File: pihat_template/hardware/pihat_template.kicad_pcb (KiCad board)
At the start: 2 copper layers, 65 x 56.5 mm, 37 parts, among them P1 CONN_01X02, P2 CONN_01X02, P3 Raspberry_Pi_+_Conn, Q1 BSS138, U1 LM3489, U2 CAT24C32HU4I-GT3, U3 FDC5614P, U4 LM1117IMPX-ADJ, U5 DMMT5401

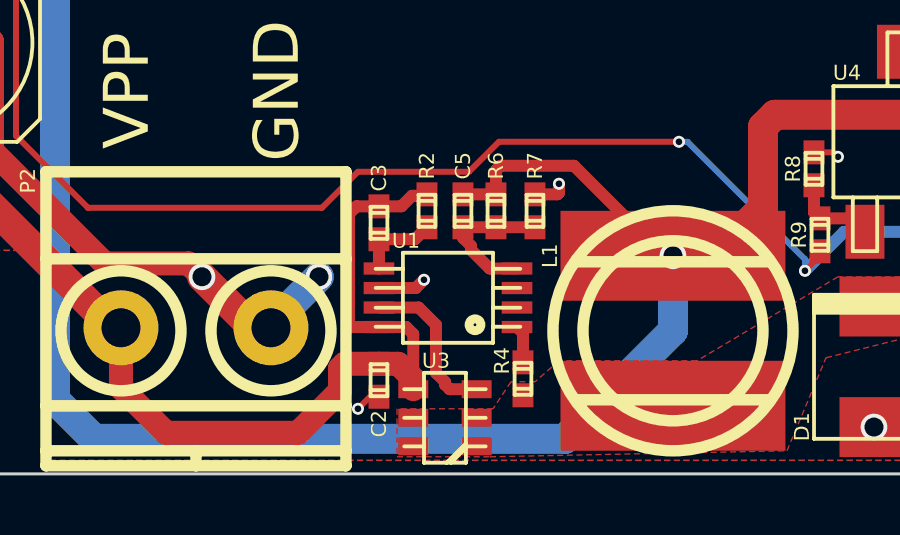
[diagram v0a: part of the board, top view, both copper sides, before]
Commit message: changed LM3489 footprint
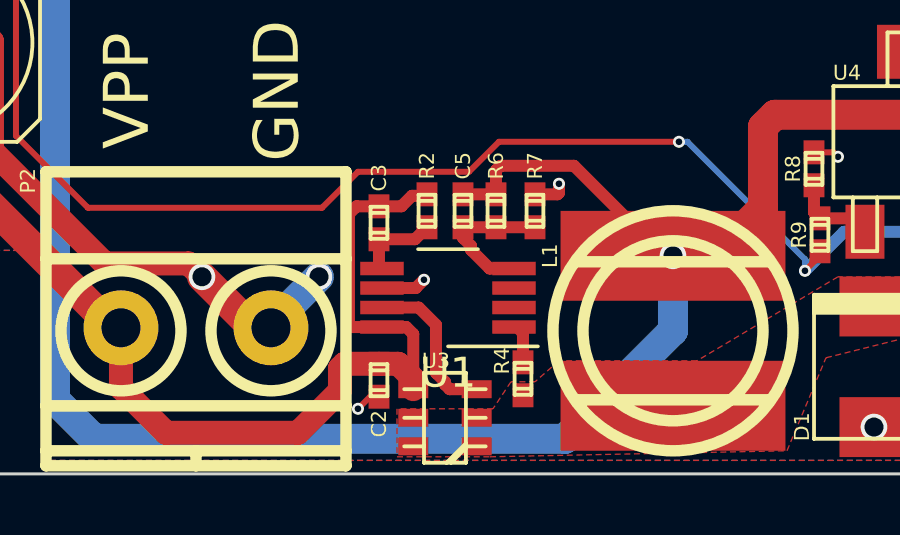
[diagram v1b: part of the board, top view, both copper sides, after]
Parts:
- U1: footprint w_smd_dil:msoic-8 -> kicad-gfa:VSSOP-8_3.0x3.0mm_Pitch0.65mm
- turned U1 to 180 degrees

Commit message: add VSSOP as a project footprint
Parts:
- U1: footprint kicad-gfa:VSSOP-8_3.0x3.0mm_Pitch0.65mm -> project:VSSOP-8_3.0x3.0mm_Pitch0.65mm
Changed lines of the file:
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@@
     )
   )
-  (module kicad-gfa:VSSOP-8_3.0x3.0mm_Pitch0.65mm (layer F.Cu)
+  (module project:VSSOP-8_3.0x3.0mm_Pitch0.65mm (layer F.Cu)
     (at 125.5 121.7 180)
     (descr "VSSOP-8 3.0 x 3.0, http://www.ti.com/lit/ds/symlink/lm75b.pdf")

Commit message: added silk UMONS-GFA + name
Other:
- board text added: "Julien M. - modified by UMONS-GFA"
- board text added: "pihat-template - 11/2017"
- board text removed: "Julien M."
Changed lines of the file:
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@@
     (area 104.1025 69.0525 177.679167 136.400001)
     (thickness 1.6)
-    (drawings 28)
+    (drawings 29)
     (tracks 280)
     (zones 0)
@@
     )
   )
+  (gr_text "pihat-template - 11/2017" (at 155.601 126.719) (layer F.SilkS)
+    (effects (font (size 0.75 0.75) (thickness 0.1875)))
+  )
   (gr_text "CERN OHL V1.2" (at 169.1 116 270) (layer B.SilkS)
     (effects (font (size 0.7 0.7) (thickness 0.175)) (justify mirror))
   )
-  (gr_text "Julien M." (at 169 116.6 90) (layer F.SilkS)
+  (gr_text "Julien M. - modified by UMONS-GFA" (at 168.8725 105.8275 90) (layer F.SilkS)
     (effects (font (size 1 1) (thickness 0.25)))
   )

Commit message: updated vias for EuroCircuits standards
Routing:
- net GND: track 44.4 -> 46.7 mm
- net Net-(JP1-Pad1): track 10.0 -> 11.5 mm
- net +3V3: track 176.1 -> 176.7 mm
- net Net-(P3-Pad28): track 32.4 -> 32.9 mm
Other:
- rule via_min_drill: 0.16 -> 0.3
- rule via_min_size: 0.26 -> 0.7

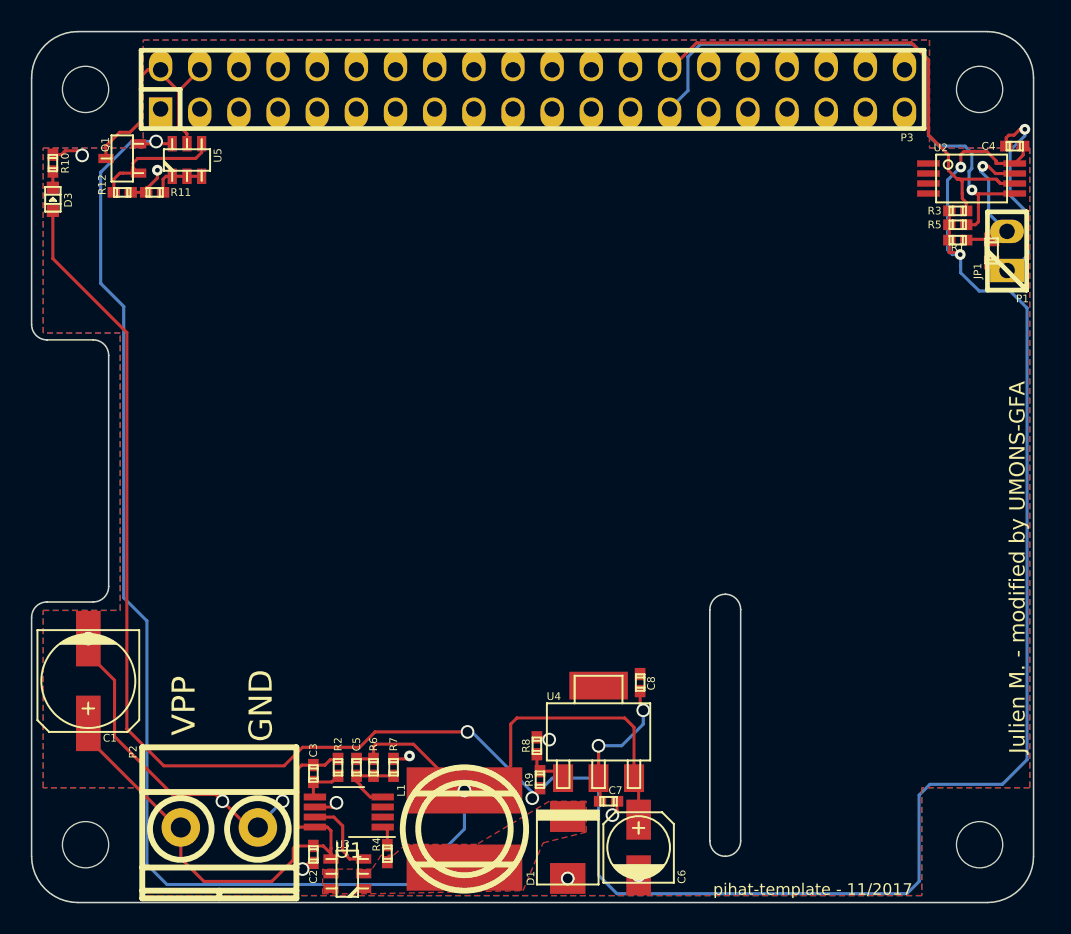
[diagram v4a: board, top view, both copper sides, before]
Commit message: added  and links to 3D models for modules in project lib
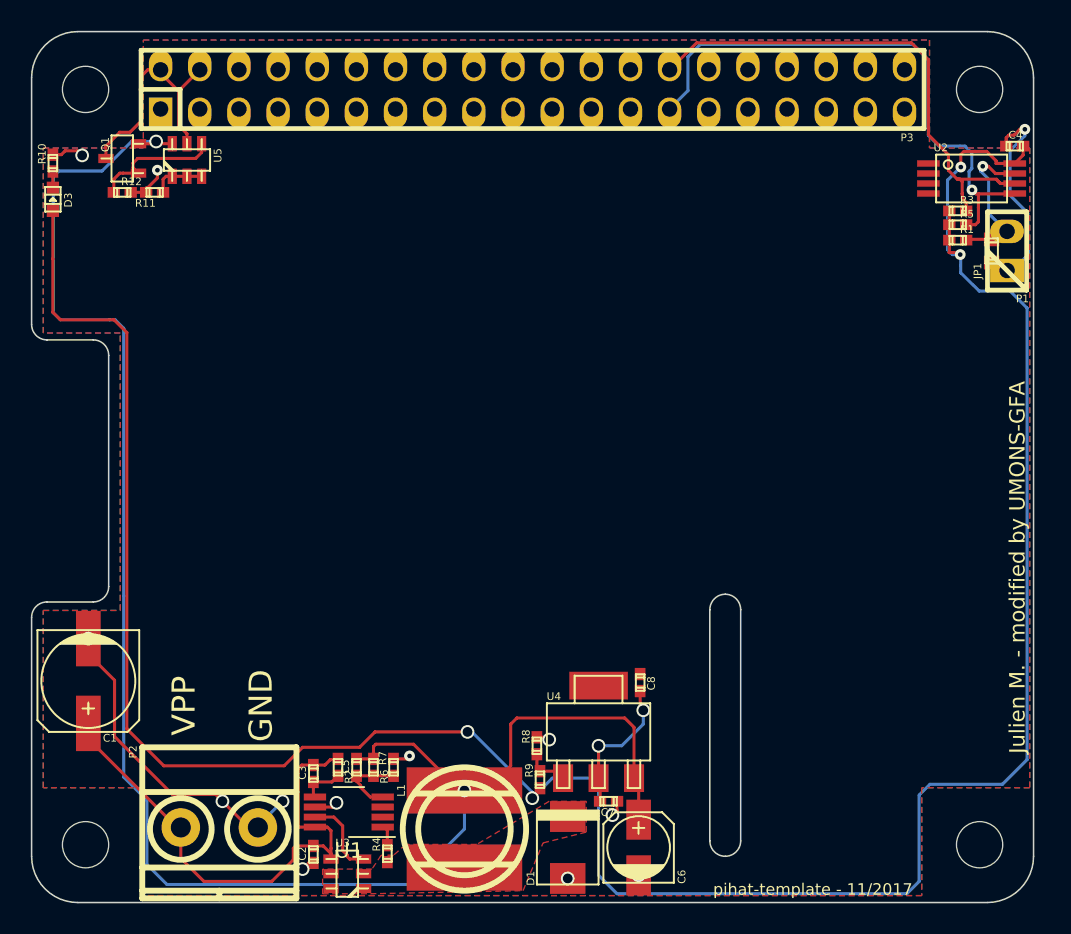
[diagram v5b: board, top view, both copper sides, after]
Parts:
- C1: footprint w_smd_cap:c_elec_6.3x7.7 -> project:c_elec_6.3x7.7
- C2, C3, C4, C5, C7, C8: footprint w_smd_cap:c_0402 -> project:c_0402
- C6: footprint w_smd_cap:c_elec_4x5.3 -> project:c_elec_4x5.3
- D1: footprint w_smd_diode:do214aa -> project:do214aa
- D3: footprint w_smd_leds:Led_0603 -> project:Led_0603
- L1: footprint w_smd_inductors:inductor_smd_8x5mm -> project:inductor_smd_8x5mm
- P1: footprint w_pin_strip:pin_strip_2 -> project:pin_strip_2
- P2: footprint w_conn_mkds:mkds_1,5-2 -> project:mkds_1,5-2
- P3: footprint w_pin_strip:pin_socket_20x2 -> project:pin_socket_20x2
- Q1: footprint w_smd_trans:sot23 -> project:sot23
- R1, R10, R11, R12, R2, R3, R4, R5, R6, R7, R8, R9: footprint w_smd_resistors:r_0402 -> project:r_0402
- U2: footprint w_smd_dil:tssop-8 -> project:tssop-8
- U3, U5: footprint w_smd_trans:sot23-6 -> project:sot23-6
- U4: footprint w_smd_trans:sot223 -> project:sot223
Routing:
- net +5V: track 108.0 -> 114.3 mm
- net +3V3: track 176.7 -> 178.7 mm

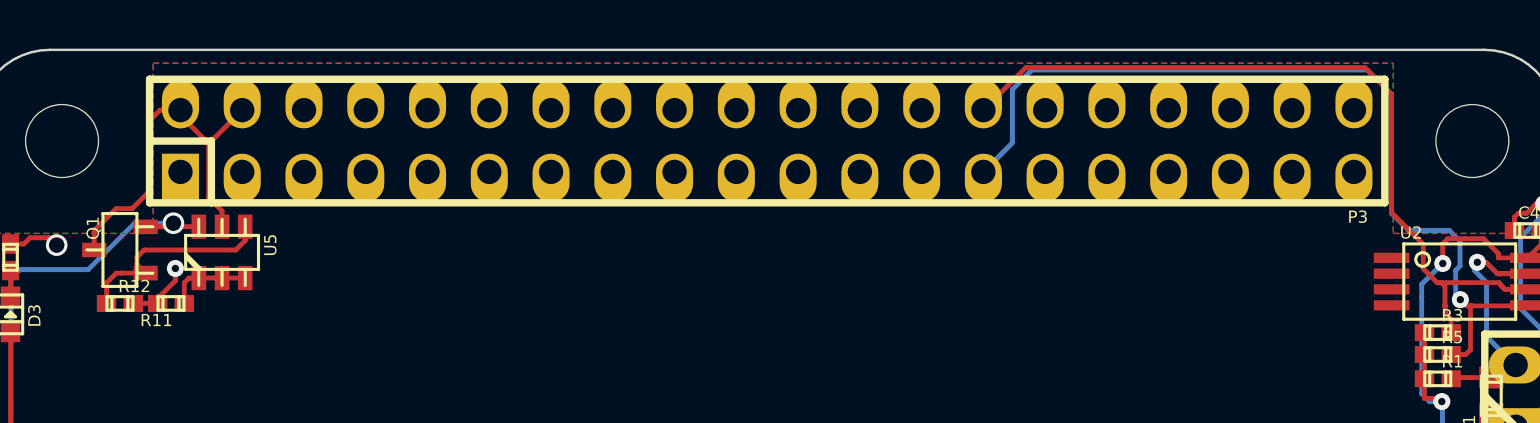
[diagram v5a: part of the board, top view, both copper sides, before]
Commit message: raspberry pi connector moved to back side of board
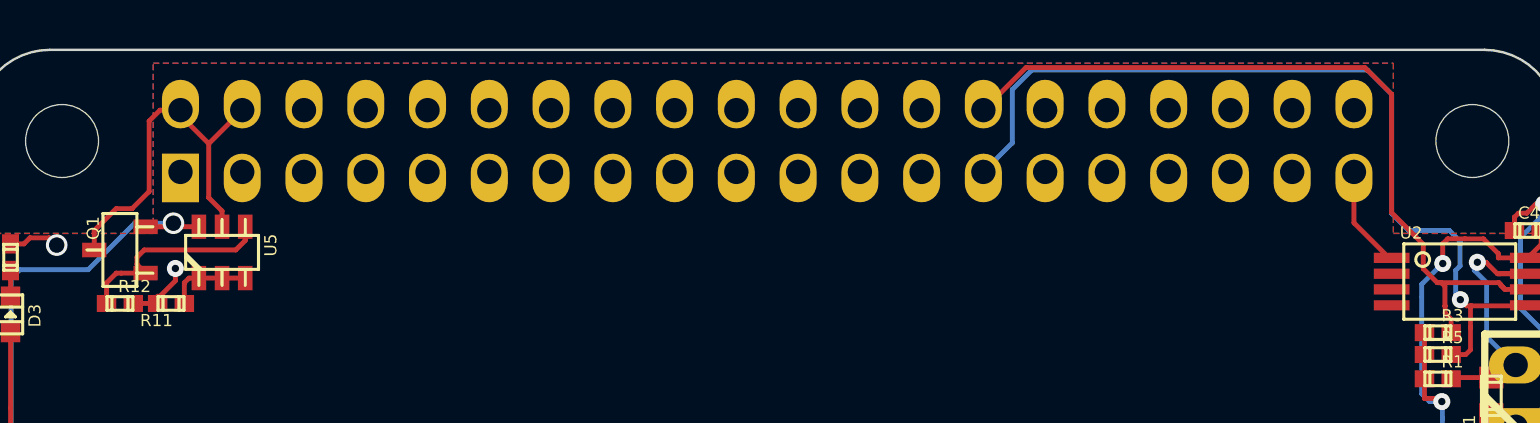
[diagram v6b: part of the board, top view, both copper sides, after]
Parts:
- P3: footprint project:pin_socket_20x2 -> project:pin_socket_20x2_mirrored; moved to B.Cu
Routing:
- net GND: track 46.7 -> 51.0 mm

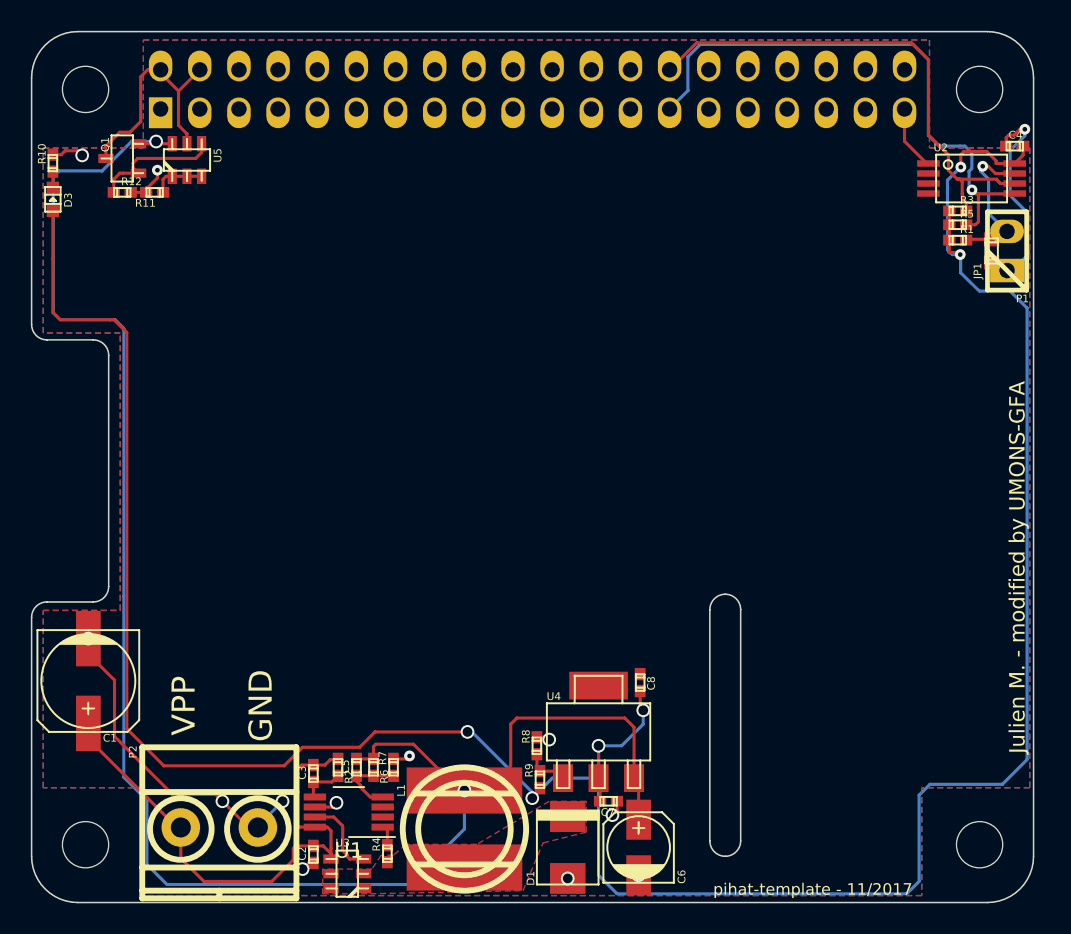
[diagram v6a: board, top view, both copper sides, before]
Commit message: refactor larger components
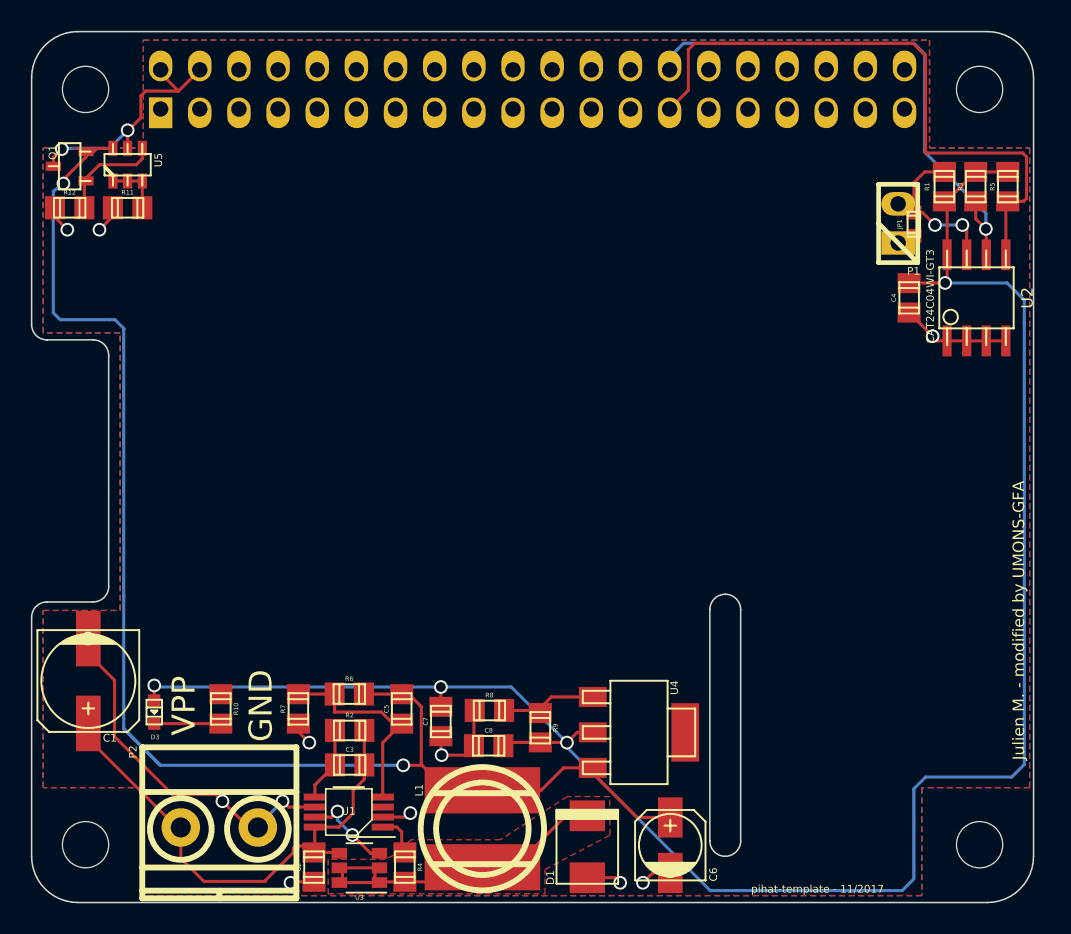
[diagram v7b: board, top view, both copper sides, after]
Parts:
- C2, C3, C4, C5, C7, C8: footprint project:c_0402 -> project:c_0805
- JP1: footprint w_smd_resistors:r_0603 -> project:r_0603
- R1, R10, R11, R12, R2, R3, R4, R5, R6, R7, R8, R9: footprint project:r_0402 -> project:r_0805
- U2: value CAT24C32HU4I-GT3 -> CAT24C04WI-GT3; footprint project:tssop-8 -> project:CAT24C04WI-GT3
- U3: footprint project:sot23-6 -> project:FDC5614P
- moved R10 37.0 mm to (117.2, 115.0)
- moved D3 33.9 mm to (112.9, 115.2), turned to 270 degrees
- moved C7 12.0 mm to (131.5, 115.8), turned to 90 degrees
- moved C4 12.0 mm to (161.8, 88.3), turned to 90 degrees
- moved C8 10.7 mm to (134.6, 117.4), turned to 0 degrees
- moved U2 7.75 mm to (166.2, 88.3), turned to 90 degrees
- moved P1 7.28 mm to (161.1, 83.5)
- moved R7 7.24 mm to (122.2, 115.0), turned to 90 degrees
- moved JP1 5.34 mm to (162.2, 83.6)
- moved R6 5.01 mm to (125.5, 114.0), turned to 0 degrees
- moved C5 4.79 mm to (128.9, 115.0)
- moved R5 4.08 mm to (168.2, 81.1), turned to 90 degrees
- moved U5 3.86 mm to (111.2, 79.7)
- moved R8 3.84 mm to (134.6, 115.1), turned to 0 degrees
- moved R1 3.58 mm to (164.1, 81.1), turned to 270 degrees
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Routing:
- net +3V3: track 178.7 -> 126.1 mm, vias 6 -> 4
- net Net-(D1-Pad2): track 0.15 -> 24.2 mm
- net +5V: track 114.3 -> 96.4 mm
- net Net-(C5-Pad2): track 5.06 -> 13.5 mm
- net Net-(P3-Pad27): track 36.5 -> 40.7 mm, vias 1 -> 0
- net Net-(D3-Pad2): track 1.05 -> 4.53 mm
- net Net-(R8-Pad1): track 2.87 -> 6.11 mm
- net Net-(C3-Pad2): track 2.74 -> 5.48 mm
- net Net-(Q1-Pad1): track 8.73 -> 6.81 mm
- net Net-(P3-Pad28): track 32.9 -> 34.8 mm, vias 0 -> 1
- net Net-(R4-Pad2): track 1.26 -> 2.69 mm
- net /Back Power Protection/5V_MCU: track 15.5 -> 16.3 mm, vias 0 -> 2
- net Net-(JP1-Pad1): track 11.5 -> 11.0 mm, vias 1 -> 2
- net GND: track 51.0 -> 50.7 mm, vias 13 -> 12
- net Net-(U1-Pad7): track 5.38 -> 5.61 mm, vias 0 -> 2
